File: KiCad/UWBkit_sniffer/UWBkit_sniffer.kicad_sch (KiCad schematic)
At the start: 1 part, among them U1 LBUA5QJ2AB

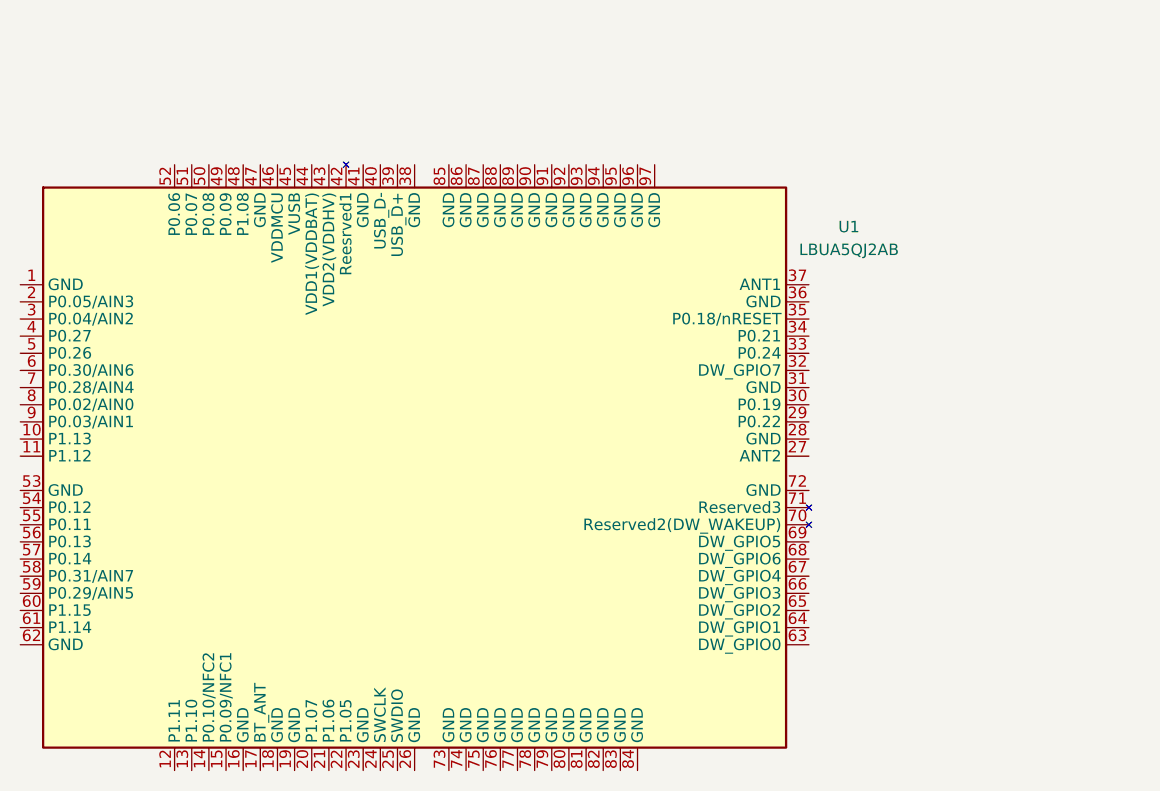
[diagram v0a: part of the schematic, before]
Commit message: Added footprint for chip antenna
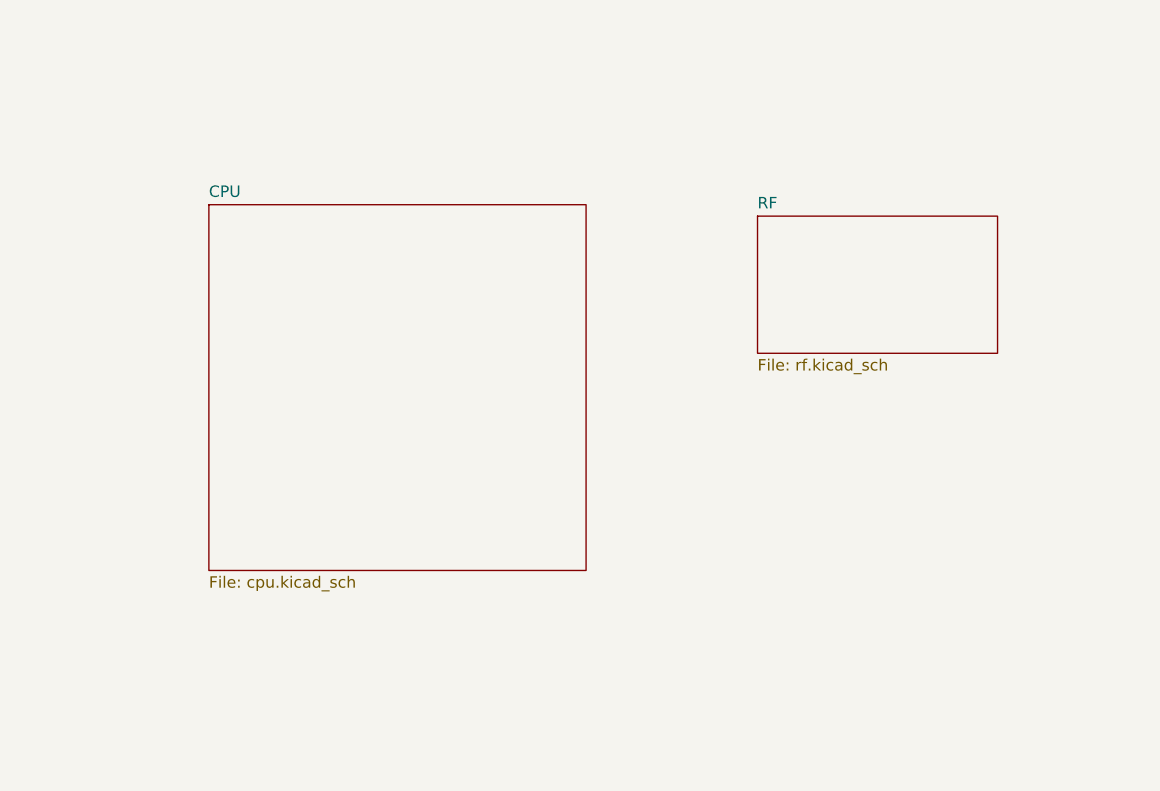
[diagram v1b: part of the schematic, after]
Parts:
- removed U1: LBUA5QJ2AB, LBUA5QJ2AB:LBUA5QJ2AB, symbol LBUA5QJ2AB:LBUA5QJ2AB
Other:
- added sheet CPU (cpu.kicad_sch)
- added sheet RF (rf.kicad_sch)

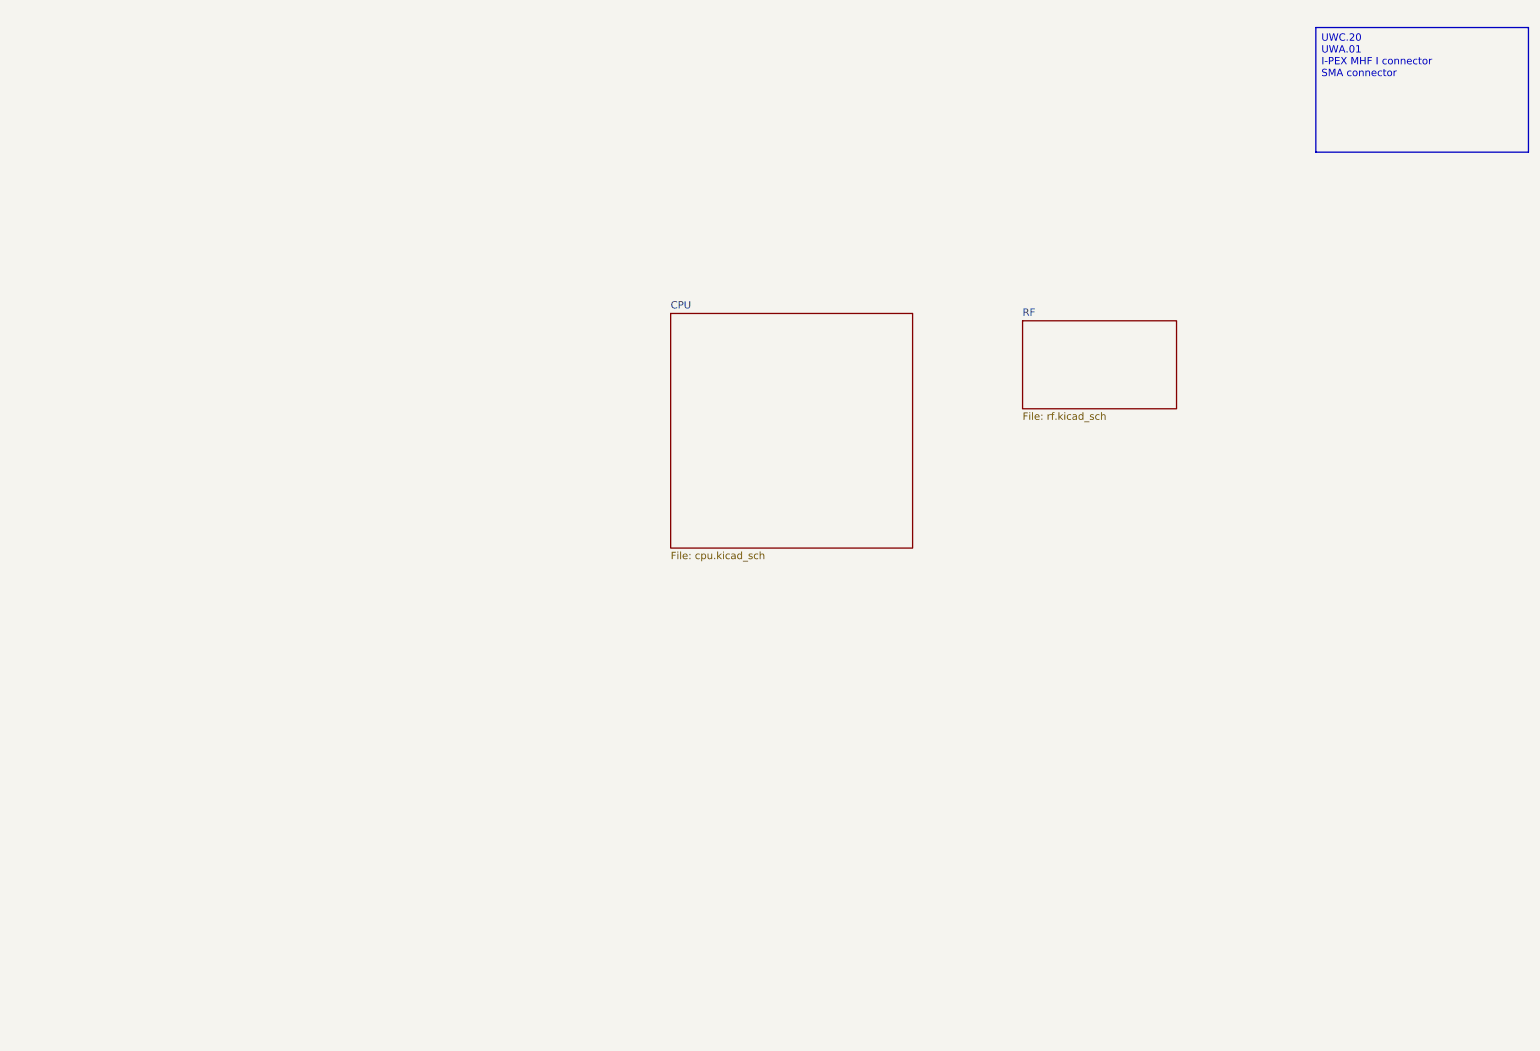
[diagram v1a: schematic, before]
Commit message: Wired connections to SoC
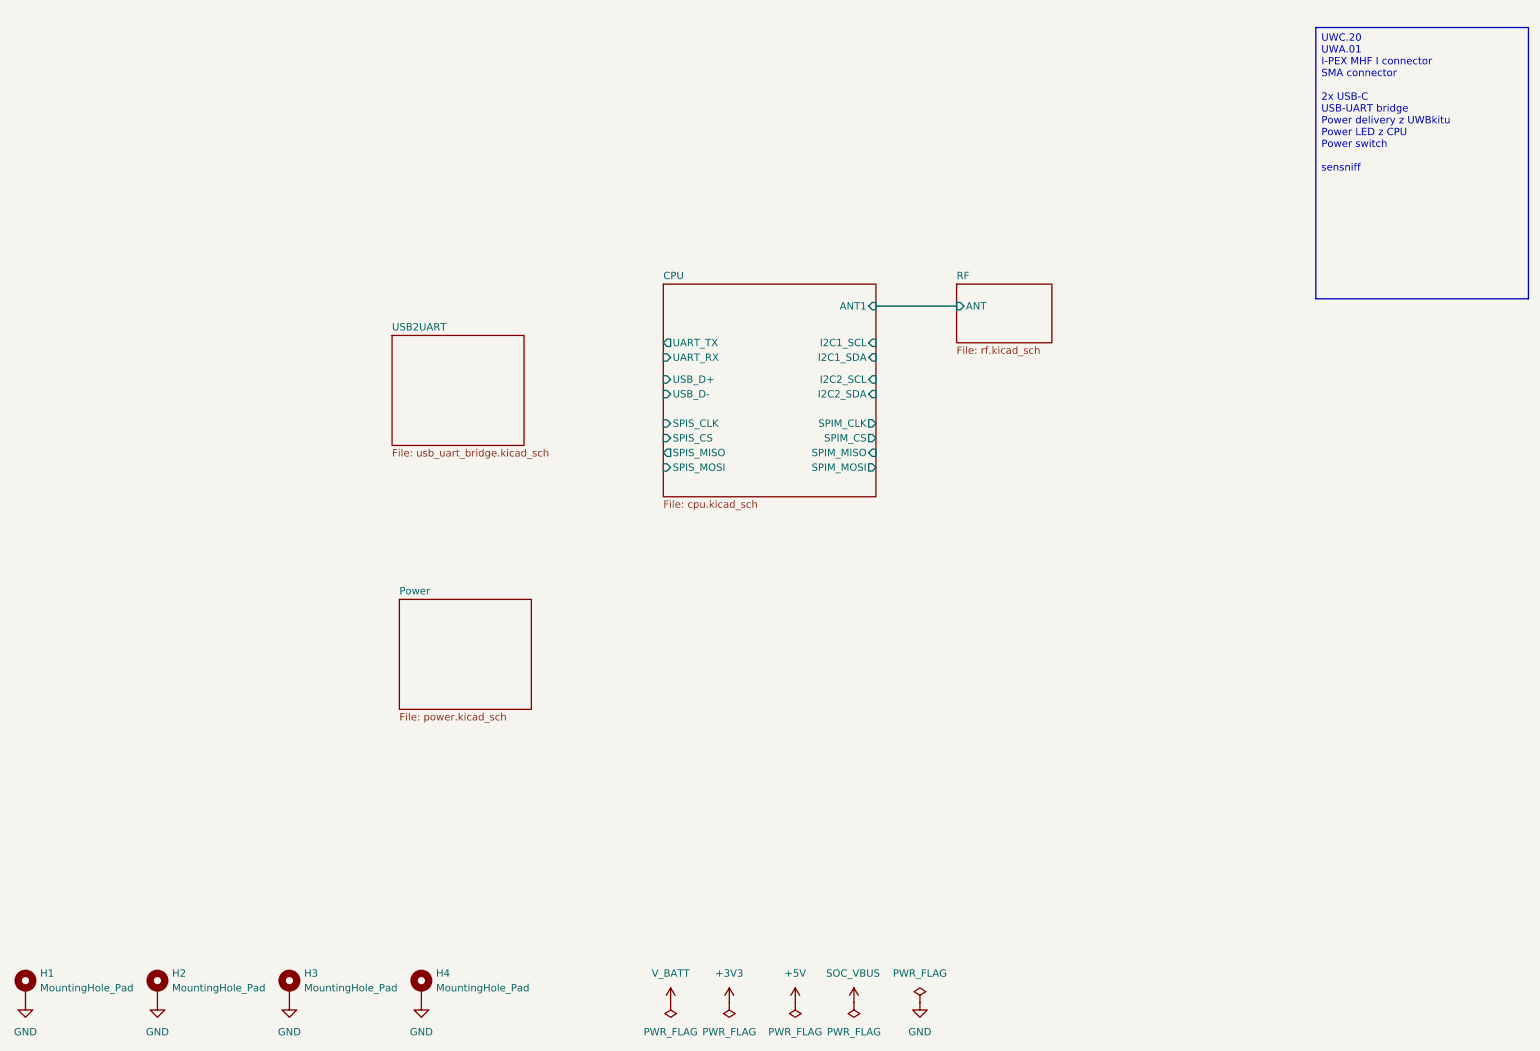
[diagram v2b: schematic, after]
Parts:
- added H1, H2, H3, H4: MountingHole_Pad, MountingHole:MountingHole_3.2mm_M3_Pad_Via, symbol Mechanical:MountingHole_Pad
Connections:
- new net GND: H1.1, H2.1, H3.1, H4.1
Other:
- added sheet Power (power.kicad_sch)
- added sheet USB2UART (usb_uart_bridge.kicad_sch)
- sheet CPU ports: added ANT1, I2C1_SCL, I2C1_SDA, I2C2_SCL, I2C2_SDA, SPIM_CLK, SPIM_CS, SPIM_MISO, SPIM_MOSI, SPIS_CLK, SPIS_CS, SPIS_MISO, SPIS_MOSI, UART_RX, UART_TX, USB_D+, USB_D-; removed none
- sheet RF ports: added ANT; removed none

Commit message: Added components to schematic
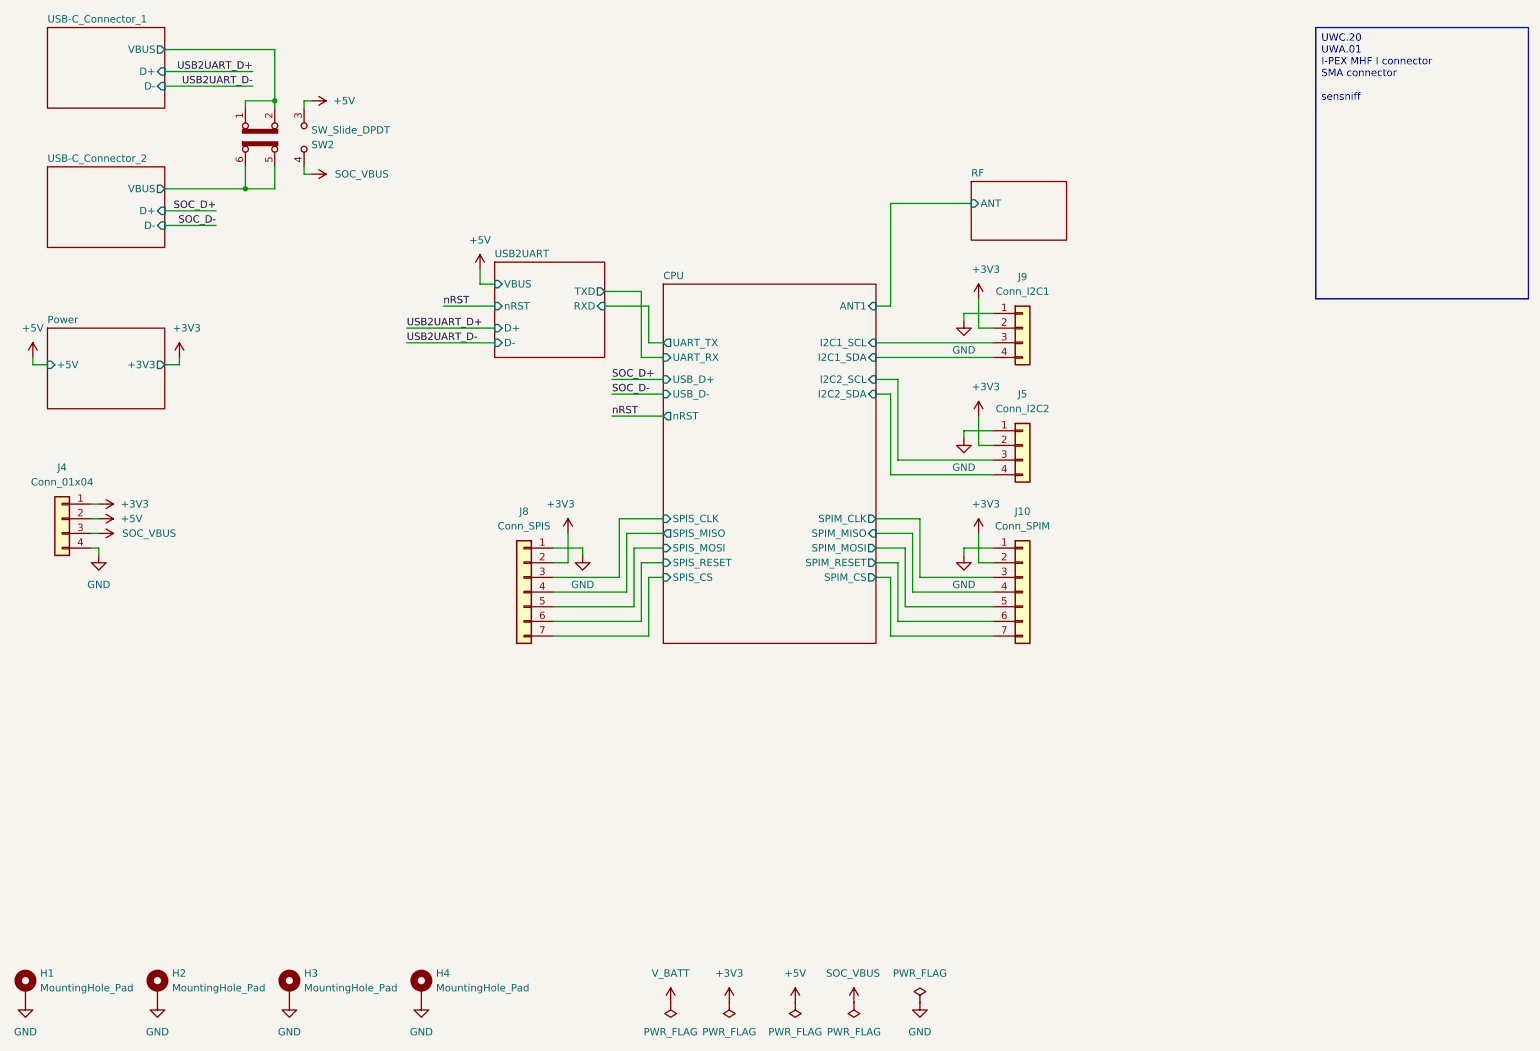
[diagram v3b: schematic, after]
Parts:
- added J10: Conn_SPIM, Connector_PinSocket_2.54mm:PinSocket_1x07_P2.54mm_Vertical, symbol Connector_Generic:Conn_01x07
- added J4: Conn_01x04, Connector_PinHeader_2.54mm:PinHeader_1x04_P2.54mm_Vertical, symbol Connector_Generic:Conn_01x04
- added J5: Conn_I2C2, Connector_PinSocket_2.54mm:PinSocket_1x04_P2.54mm_Vertical, symbol Connector_Generic:Conn_01x04
- added J8: Conn_SPIS, Connector_PinSocket_2.54mm:PinSocket_1x07_P2.54mm_Vertical, symbol Connector_Generic:Conn_01x07
- added J9: Conn_I2C1, Connector_PinSocket_2.54mm:PinSocket_1x04_P2.54mm_Vertical, symbol Connector_Generic:Conn_01x04
- added SW2: SW_Slide_DPDT, Button_Switch_THT:SW_CK_JS202011CQN_DPDT_Straight, symbol Switch:SW_Slide_DPDT
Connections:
- net +3V3: now also J10.2 (Pin_2), J4.1 (Pin_1), J5.2 (Pin_2), J8.2 (Pin_2), J9.2 (Pin_2)
- net +5V: now also J4.2 (Pin_2), SW2.3 (C)
- net CPU/I2C1_SCL: now also J9.3 (Pin_3)
- net CPU/I2C1_SDA: now also J9.4 (Pin_4)
- net CPU/I2C2_SCL: now also J5.3 (Pin_3)
- net CPU/I2C2_SDA: now also J5.4 (Pin_4)
- net CPU/SPIM_CLK: now also J10.3 (Pin_3)
- net CPU/SPIM_CS: now also J10.7 (Pin_7)
- net CPU/SPIM_MISO: now also J10.4 (Pin_4)
- net CPU/SPIM_MOSI: now also J10.5 (Pin_5)
- net CPU/SPIS_CLK: now also J8.3 (Pin_3)
- net CPU/SPIS_CS: now also J8.7 (Pin_7)
- net CPU/SPIS_MISO: now also J8.4 (Pin_4)
- net CPU/SPIS_MOSI: now also J8.5 (Pin_5)
- net GND: now also J10.1 (Pin_1), J4.4 (Pin_4), J5.1 (Pin_1), J8.1 (Pin_1), J9.1 (Pin_1)
- net SOC_VBUS: now also J4.3 (Pin_3), SW2.4 (A)
- new net CPU/SPIM_RESET: J10.6 (Pin_6)
- new net CPU/SPIS_RESET: J8.6 (Pin_6)
- new net USB-C_Connector_1/VBUS: SW2.1 (A), SW2.2 (B)
- new net USB-C_Connector_2/VBUS: SW2.5 (B), SW2.6 (C)
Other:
- added sheet USB-C_Connector_1 (usb_c.kicad_sch)
- added sheet USB-C_Connector_2 (usb_c.kicad_sch)
- sheet CPU ports: added SPIM_RESET, SPIS_RESET, nRST; removed none
- sheet Power ports: added +3V3, +5V; removed none
- sheet USB2UART ports: added D+, D-, RXD, TXD, VBUS, nRST; removed none

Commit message: First version of PCB
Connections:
- net +5V: now also SW2.4 (A); no longer SW2.3 (C)
- net SOC_VBUS: now also SW2.3 (C); no longer SW2.4 (A)
- net USB-C_Connector_1/VBUS: now also SW2.5 (B), SW2.6 (C); no longer SW2.1 (A), SW2.2 (B)
- net USB-C_Connector_2/VBUS: now also SW2.1 (A), SW2.2 (B); no longer SW2.5 (B), SW2.6 (C)
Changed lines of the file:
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@@
 		(lib_id "Switch:SW_Slide_DPDT")
 		(at 59.69 38.1 90)
-		(mirror x)
 		(unit 1)
 		(exclude_from_sim no)
@@
 		(dnp no)
 		(property "Reference" "SW2"
-			(at 66.04 39.3701 90)
+			(at 66.04 36.8299 90)
 			(effects
 				(font
@@
 		)
 		(property "Value" "SW_Slide_DPDT"
-			(at 66.04 36.8301 90)
+			(at 66.04 39.3699 90)
 			(effects
 				(font
@@
 		)
 		(property "Footprint" "Button_Switch_THT:SW_CK_JS202011CQN_DPDT_Straight"
-			(at 54.61 52.07 0)
+			(at 54.61 24.13 0)
 			(effects
 				(font
